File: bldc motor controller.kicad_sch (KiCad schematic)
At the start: 8 parts

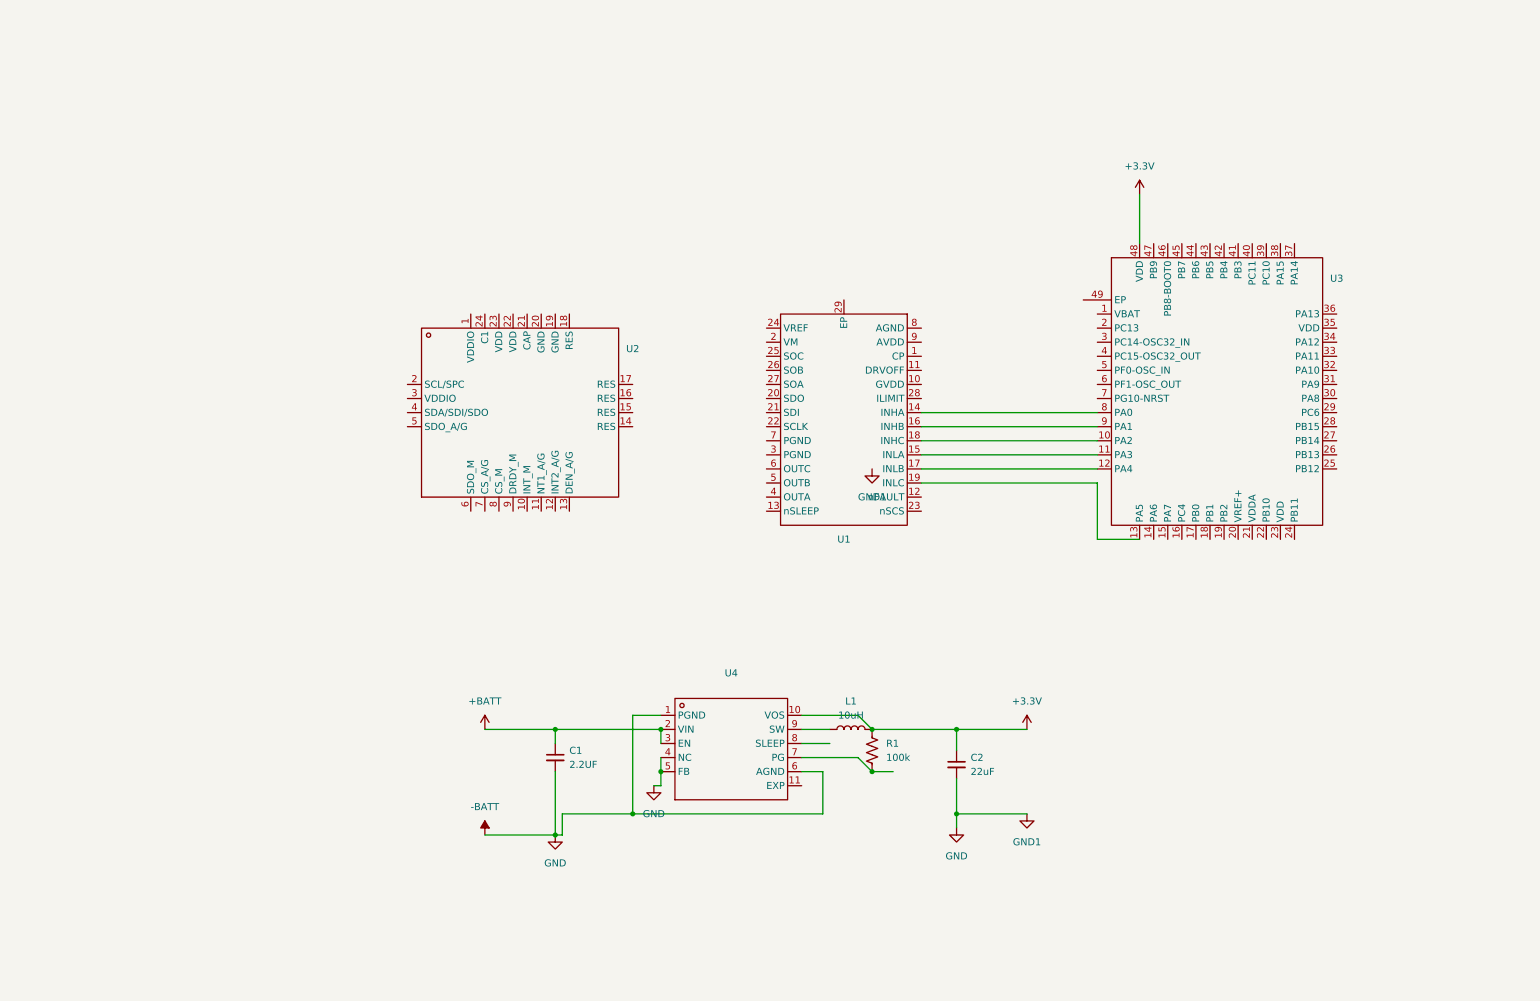
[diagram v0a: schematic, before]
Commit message: did a lot of work, swapped out basically every chip at least once. Good times. Need to actually use global frames like EFR
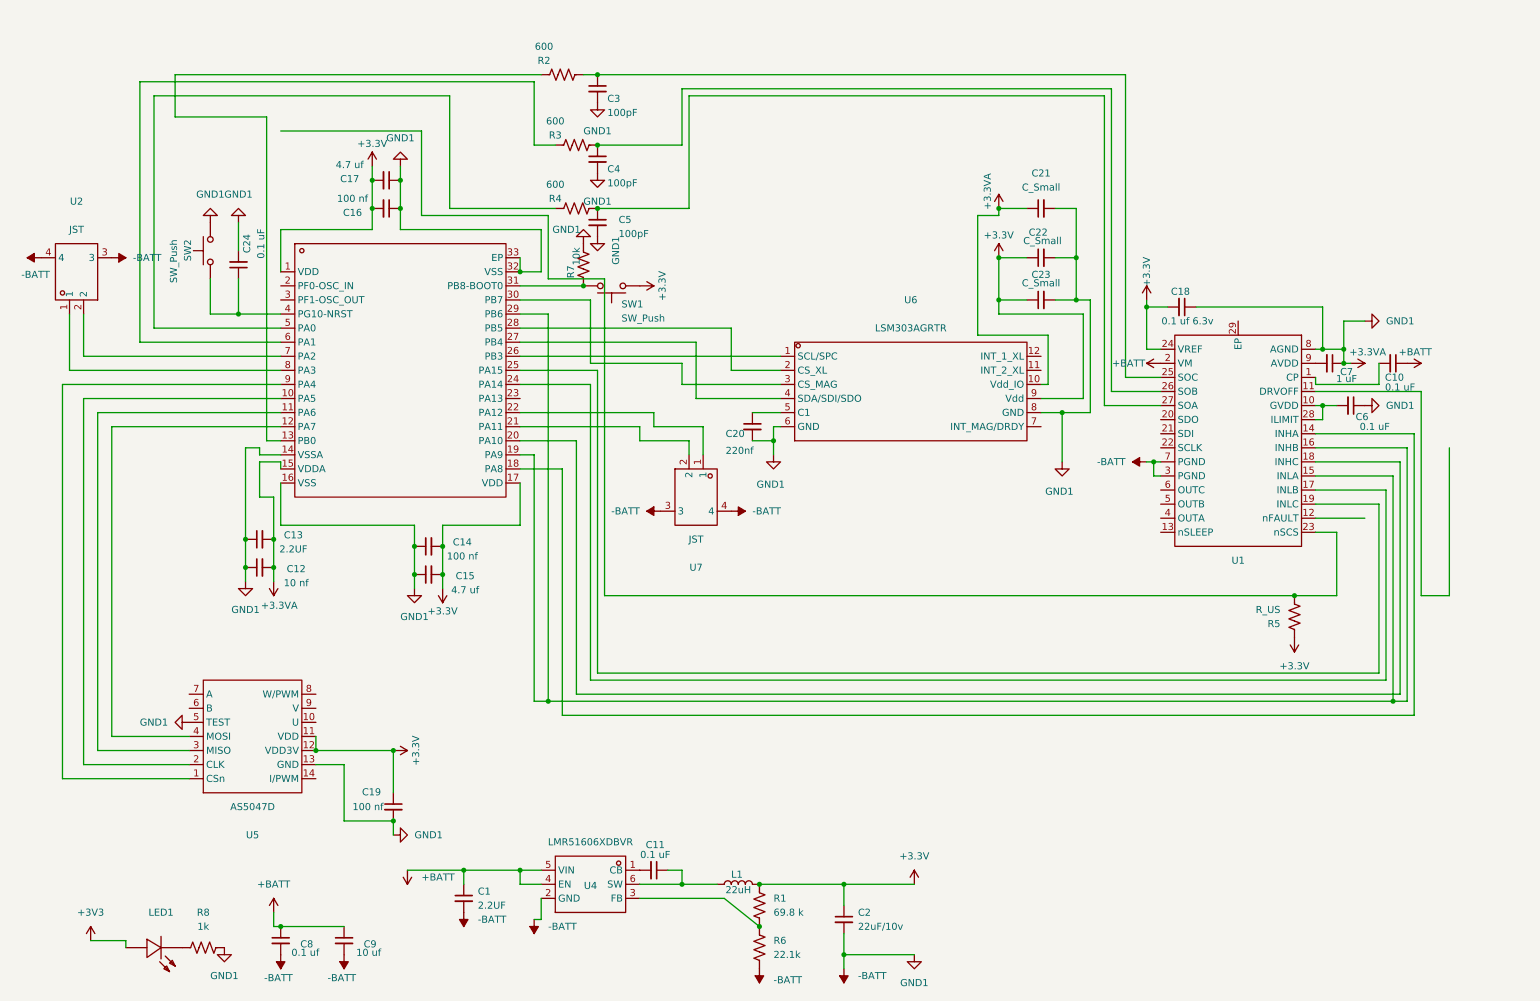
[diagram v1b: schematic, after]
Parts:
- removed U2: ~, ProLib_pcs_2025-09-24 (1):LGA-24_L3.5-W3.0-P0.43-TL, symbol bldc controller:LSM9DS1TR
- removed U3: ~, ProLib_pcs_2025-09-24 (2):VQFN-48_L7.0-W7.0-P0.50-BL-EP5.5, symbol bldc controller:STM32G431CBU6
- removed U4: ~, ProLib_pcs_2025-09-24 (3):WSON-10_L3.0-W2.0-P0.50-BL-EP, symbol bldc controller:TPS62175DQCR
- added C10, C11, C24, C6: 0.1 uF, symbol Device:C_Small
- added C12: 10 nf, symbol Device:C_Small
- added C13: 2.2UF, symbol Device:C_Small
- added C14, C16, C19: 100 nf, symbol Device:C_Small
- added C15, C17: 4.7 uf, symbol Device:C_Small
- added C18: 0.1 uf 6.3v, symbol Device:C_Small
- added C20: 220nf, symbol Device:C_Small
- added C21, C22, C23: C_Small, symbol Device:C_Small
- added C3, C4, C5: 100pF, symbol Device:C_Small
- added C7: 1 uF, symbol Device:C_Small
- added C8: 0.1 uf, symbol Device:C_Small
- added C9: 10 uf, symbol Device:C_Small
- added LED1: ~, ProLib_pcs_2025-10-01 (3):LED0603-RD, symbol bldc controller:KT-0603R
- added R2, R3, R4: 600, symbol Device:R_US
- added R5: R_US, symbol Device:R_US
- added R6: 22.1k, symbol Device:R_US
- added R7: 10k, symbol Device:R_US
- added R8: 1k, symbol Device:R_US
- added SW1, SW2: SW_Push, symbol Switch:SW_Push
- added U2, U7: ~, ProLib_pcs_2025-10-01 (1):CONN-SMD_SM02B-GHS-TB-LF-SN, symbol bldc controller:SM02B-GHS-TB(LF)(SN)
- added U3: ~, ProLib_pcs_2025-10-01:QFN-32_L5.0-W5.0-P0.50-BL-EP3.7, symbol bldc controller:STM32G431KBU6
- added U4: ~, 48v-3.3v buck:SOT-23-6_L2.9-W1.6-P0.95-LS2.8-BR, symbol bldc controller:LMR51606XDBVR
- added U5: ~, ProLib_pcs_2025-10-01:TSSOP-14_L5.0-W4.4-P0.65-LS6.4-BL, symbol bldc controller:AS5047D-ATSM
- added U6: ~, ProLib_pcs_2025-10-01 (2):LGA-12_L2.0-W2.0-P0.50-BL, symbol bldc controller:LSM303AGRTR
- C2: value 22uF -> 22uF/10v
- L1: value 10uH -> 22uH
- R1: value 100k -> 69.8 k
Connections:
- net -BATT is gone; now on net +3.3VA: C1.2, C2.2
- net +3.3V: now also U1.24 (VREF), C14.2, C15.2, C16.2, C17.2, C18.2, C19.1, C22.1, C23.1, R5.1, SW1.1, U3.1 (VDD), U3.17 (VDD), U5.11 (VDD), U5.12 (VDD3V), U6.9 (Vdd)
- net +BATT: now also U1.2 (VM), C10.1, C8.1, C9.1, U4.4 (EN), U4.5 (VIN)
- net at L1.1: now also C11.1, U4.6 (SW)
- net at U1.1 (CP): now also C10.2
- net at U1.10 (GVDD): now also U1.28 (ILIMIT), C6.2
- net at U1.14 (INHA): now also U3.18 (PA8)
- net at U1.15 (INLA): now also U1.16 (INHB), U3.19 (PA9), U3.29 (PB6)
- net at U1.17 (INLB): now also U3.24 (PA14)
- net at U1.18 (INHC): now also U3.20 (PA10)
- net at U1.19 (INLC): now also U3.25 (PA15)
- net at U1.23 (nSCS): now also R5.2
- net at U1.25 (SOC): now also C3.1, R2.1
- net at U1.26 (SOB): now also C4.1, R3.1
- net at U1.27 (SOA): now also C5.1, R4.1
- net +3.3VA: now reaches U1.3 (PGND)
- net +3.3VA: now also U1.7 (PGND), U1.8 (AGND), C12.1, C12.2, C13.1, C13.2, C14.1, C15.1, C16.1, C17.1, C18.1, C19.2, C20.2, C21.1, C21.2, C22.2, C23.2, C24.2, C3.2, C4.2, C5.2, C6.1, C7.1, C8.2, C9.2, R6.2, R7.2, R8.2, SW2.2, U2.3, U2.4, U3.14 (VSSA), U3.15 (VDDA), U3.16 (VSS), U3.32 (VSS), U3.33 (EP), U4.2 (GND), U5.13 (GND), U5.5 (TEST), U6.10 (Vdd_IO), U6.6 (GND), U6.8 (GND), U7.3, U7.4
- net at U1.9 (AVDD): now also C7.2
- net at R1.2: now also R6.1, U4.3 (FB)
- new net: R2.2, U3.13 (PB0)
- new net: LED1.1 (K), R8.1
- new net: R3.2, U3.6 (PA1)
- new net: U3.26 (PB3), U6.1 (SCL/SPC)
- new net: U3.28 (PB5), U6.2 (CS_XL)
- new net: U3.30 (PB7), U6.3 (CS_MAG)
- new net: U3.27 (PB4), U6.4 (SDA/SDI/SDO)
- new net: C20.1, U6.5 (C1)
- new net: U3.9 (PA4), U5.1 (CSn)
- new net: U3.10 (PA5), U5.2 (CLK)
- new net: U3.11 (PA6), U5.3 (MISO)
- new net: U3.12 (PA7), U5.4 (MOSI)
- new net: C24.1, SW2.1, U3.4 (PG10-NRST)
- new net: U3.22 (PA12), U7.1
- new net: U3.21 (PA11), U7.2
- new net: U2.1, U3.8 (PA3)
- new net: U2.2, U3.7 (PA2)
- new net: R7.1, SW1.2, U3.31 (PB8-BOOT0)
- new net: R4.2, U3.5 (PA0)
- new net: C11.2, U4.1 (CB)
- new net +3V3: LED1.2 (A)
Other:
- moved on the sheet: C1, C2, L1, R1, U1

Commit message: fuck yeah is closing in
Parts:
- removed R5: R_US, symbol Device:R_US
- removed SW1, SW2: SW_Push, symbol Switch:SW_Push
- removed U1: ~, ProLib_pcs_2025-09-24:VQFN-28_L6.0-W5.0-P0.50-TL-EP4.0, symbol bldc controller:DRV8376SNLGR
- removed U2: ~, ProLib_pcs_2025-10-01 (1):CONN-SMD_SM02B-GHS-TB-LF-SN, symbol bldc controller:SM02B-GHS-TB(LF)(SN)
- added CN1: ~, Connector_JST:JST_EH_B2B-EH-A_1x02_P2.50mm_Vertical, symbol bldc controller:WAFER-XH254WZ-2AM
- added R10, R11, R9: 2000, Resistor_SMD:R_01005_0402Metric, symbol Device:R_US
- added SW1, SW2: ~, bldc-motor-footprints:KEY-SMD_4P-L2.6-W1.6-P0.80-LS3.0, symbol bldc controller:SKTAACE010
- added U1: ~, bldc-motor-footprints:VQFN-28_L6.0-W5.0-P0.50-TL-EP4.0, symbol bldc controller:DRV8376HNLGR
- added U2: ~, bldc-motor-footprints:CONN-SMD_4P-P1.25_SM04B-GHS-TB-LF-SN, symbol bldc controller:SM04B-GHS-TB(LF)(SN)
- added U8: ~, Button_Switch_THT:SW_Slide-03_Wuerth-WS-SLTV_10x2.5x6.4_P2.54mm, symbol bldc controller:MR30-M
- C1: footprint (none) -> Capacitor_SMD:C_1206_3216Metric
- C10, C11, C18, C19, C24, C8: footprint (none) -> Capacitor_SMD:C_0402_1005Metric
- C12, C13, C14, C15, C16, C17, C20, C21, C22, C23, C3, C4, C5, C6: footprint (none) -> Capacitor_SMD:C_01005_0402Metric
- C2, R1: footprint (none) -> Capacitor_SMD:C_0805_2012Metric
- C7, C9: footprint (none) -> Capacitor_SMD:C_0603_1608Metric
- L1: footprint (none) -> Inductor_SMD:L_Bourns_SRP5030T
- LED1: footprint ProLib_pcs_2025-10-01 (3):LED0603-RD -> bldc-motor-footprints:LED0603-RD
- R2, R3, R4: footprint (none) -> Resistor_SMD:R_01005_0402Metric
- R6, R8: footprint (none) -> Resistor_SMD:R_0603_1608Metric
- R7: footprint (none) -> Resistor_SMD:R_0402_1005Metric
- U3: footprint ProLib_pcs_2025-10-01:QFN-32_L5.0-W5.0-P0.50-BL-EP3.7 -> bldc-motor-footprints:QFN-32_L5.0-W5.0-P0.50-BL-EP3.7
- U4: footprint 48v-3.3v buck:SOT-23-6_L2.9-W1.6-P0.95-LS2.8-BR -> bldc-motor-footprints:SOT-23-6_L2.9-W1.6-P0.95-LS2.8-BR
- U5: footprint ProLib_pcs_2025-10-01:TSSOP-14_L5.0-W4.4-P0.65-LS6.4-BL -> bldc-motor-footprints:TSSOP-14_L5.0-W4.4-P0.65-LS6.4-BL
- U6: footprint ProLib_pcs_2025-10-01 (2):LGA-12_L2.0-W2.0-P0.50-BL -> bldc-motor-footprints:LGA-12_L2.0-W2.0-P0.50-BL
- U7: footprint ProLib_pcs_2025-10-01 (1):CONN-SMD_SM02B-GHS-TB-LF-SN -> bldc-motor-footprints:CONN-SMD_SM02B-GHS-TB-LF-SN
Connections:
- net +3V3 is gone; now on net +3.3V: LED1.2 (A)
- net +3.3V: now also C12.2, C13.2, C21.1, U3.15 (VDDA), U6.10 (Vdd_IO), SW2.3, U1.24 (VREF), U2.3
- net +3.3VA: now also CN1.1, R10.2, R11.2, R9.2, SW1.1, U1.11 (DRVOFF), U1.2 (VM), U1.22 (SCLK/SLEW), U1.29 (EP), U1.8 (AGND), U2.4, U2.5, U2.6; no longer C12.2, C13.2, C21.1, U3.15 (VDDA), U6.10 (Vdd_IO)
- net +BATT: now also CN1.2, U1.3 (PGND), U1.7 (PGND)
- net at C3.1, R2.1: now also U1.27 (SOA)
- net SOA: now reaches R2.2
- net SOA: now also U3.5 (PA0); no longer U3.13 (PB0)
- net at C4.1, R3.1: now also U1.26 (SOB)
- net SOB: now reaches R3.2, U3.6 (PA1)
- net ENAB_XL: now reaches U3.26 (PB3)
- net ENAB_XL: now also U6.2 (CS_XL); no longer U6.1 (SCL/SPC)
- net MOSI1: now reaches U3.28 (PB5)
- net MOSI1: now also U5.4 (MOSI); no longer U6.2 (CS_XL)
- net at U3.30 (PB7): no longer U6.3 (CS_MAG)
- net at U3.27 (PB4): no longer U6.4 (SDA/SDI/SDO)
- net NSS1: now reaches U3.9 (PA4), U5.1 (CSn)
- net SCK1: now reaches U3.10 (PA5), U5.2 (CLK)
- net MISO1: now reaches U5.3 (MISO)
- net MISO1: now also U3.29 (PB6); no longer U3.11 (PA6)
- net TIM1_CH1N: now reaches U3.12 (PA7)
- net TIM1_CH1N: now also U1.15 (INLA); no longer U5.4 (MOSI)
- net TI_AVDD: now reaches C7.2
- net TI_AVDD: now also U1.13 (nSLEEP), U1.9 (AVDD)
- net Reset: now reaches C24.1, U3.4 (PG10-NRST)
- net Reset: now also SW1.2
- net CAN_RX: now reaches U7.1
- net CAN_RX: now also U3.21 (PA11); no longer U3.22 (PA12)
- net CAN_TX: now reaches U7.2
- net CAN_TX: now also U3.22 (PA12); no longer U3.21 (PA11)
- net at C10.2: now also U1.1 (CP)
- net I-LIMIT: now reaches C6.2
- net I-LIMIT: now also U1.10 (GVDD), U1.28 (ILIMIT)
- net TIM1_CH1: now reaches U3.18 (PA8)
- net TIM1_CH1: now also U1.14 (INHA)
- net TIM1_CH2: now reaches U3.19 (PA9)
- net TIM1_CH2: now also U1.16 (INHB); no longer U3.29 (PB6)
- net SDA1: now reaches U3.24 (PA14)
- net SDA1: now also U6.4 (SDA/SDI/SDO)
- net TIM1_CH3: now reaches U3.20 (PA10)
- net TIM1_CH3: now also U1.18 (INHC)
- net ENAB_MAG: now reaches U3.25 (PA15)
- net ENAB_MAG: now also U6.3 (CS_MAG)
- net at C5.1, R4.1: now also U1.25 (SOC)
- net UART_RX: now reaches U3.8 (PA3)
- net UART_RX: now also U2.2
- net UART_TX: now reaches U3.7 (PA2)
- net UART_TX: now also U2.1
- net TIM1_CH3N: now reaches U3.2 (PF0-OSC_IN)
- net TIM1_CH3N: now also U1.19 (INLC)
- net SCL1: now reaches U3.23 (PA13)
- net SCL1: now also U6.1 (SCL/SPC)
- net TI_FAULT: now reaches U3.3 (PF1-OSC_OUT)
- net TI_FAULT: now also U1.12 (nFAULT)
- net BOOT0: now reaches R7.1, U3.31 (PB8-BOOT0)
- net BOOT0: now also SW2.4
- net SOC: now reaches R4.2
- net SOC: now also U3.11 (PA6); no longer U3.5 (PA0)
- new net: R9.1, U1.21 (SDI/GAIN)
- new net: R10.1, U1.20 (SDO/MODE_SR)
- new net: R11.1, U1.23 (nSCS/OCP)
- new net PHASE-A: U1.4 (OUTA), U8.1
- new net PHASE-B: U1.5 (OUTB), U8.2
- new net PHASE-C: U1.6 (OUTC), U8.3
- new net TIM1_CH2N: U1.17 (INLB), U3.13 (PB0)
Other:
- moved on the sheet: C1, C10, C11, C12, C13, C14, C15, C16, C17, C18, C19, C2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
